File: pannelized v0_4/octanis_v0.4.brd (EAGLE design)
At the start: 69.2 x 41.9 mm, 69 parts, among them IC1 BME280, Q2 32.768kHz, U3 DRV8836DSSR, U4 DRV8836DSSR, U5 DRV8836DSSR, U7 DRV8836DSSR

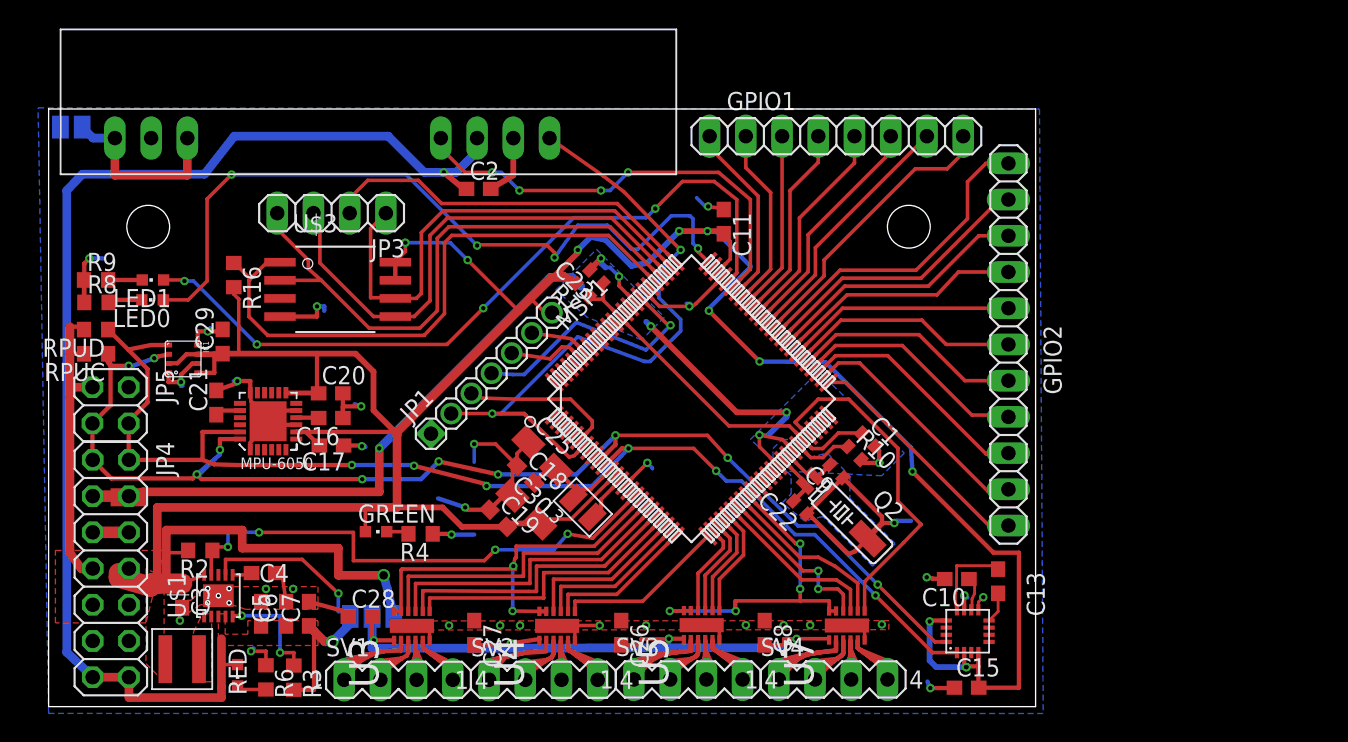
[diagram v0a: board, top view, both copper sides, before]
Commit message: corrected I2C SDA short to 3V
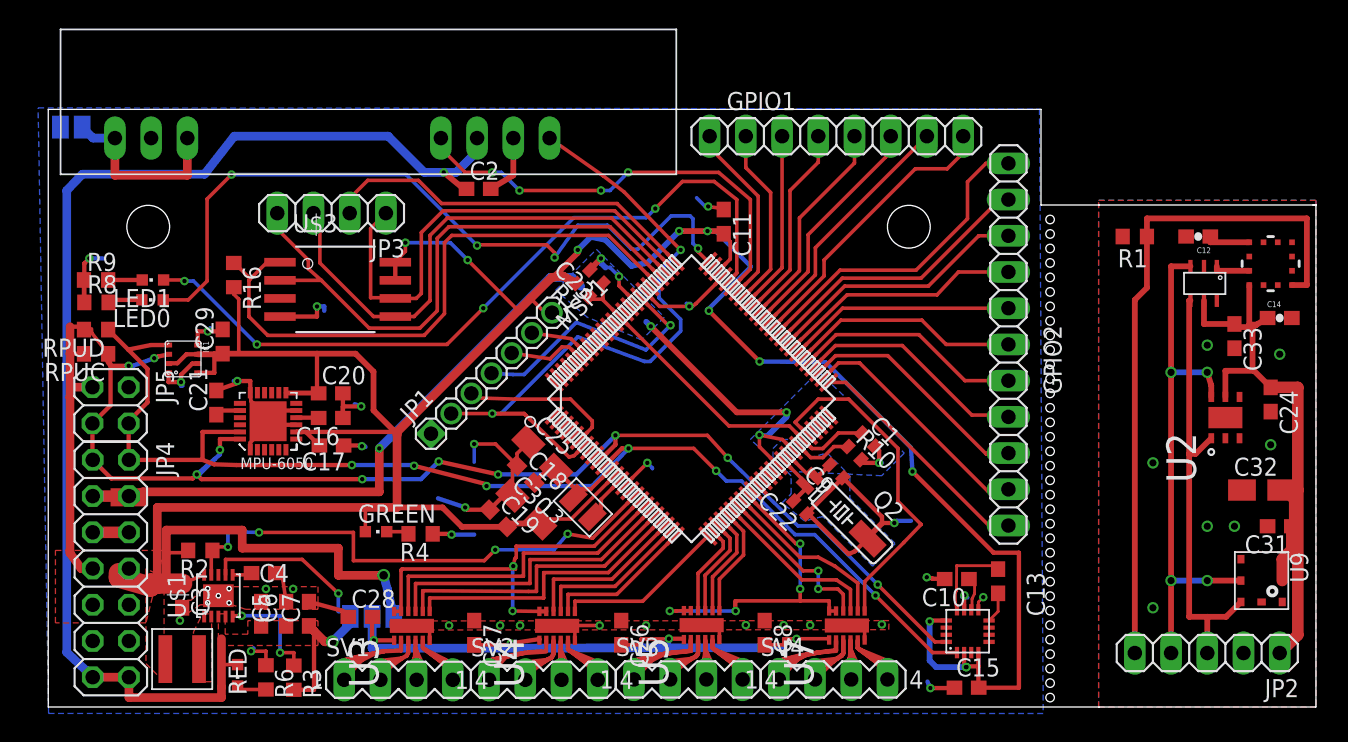
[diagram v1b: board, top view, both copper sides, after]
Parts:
- added C12: 1nF, SparkFun-Capacitors:0603-CAP
- added C14: 0.1uF, SparkFun-Capacitors:0603-CAP
- added C24, C31, C33: 100n, rcl:C0603
- added C32: 10u, resistor:A/3216-18R
- added JP2: (no value), Headerlibrary:1X05
- added R1: 10k, resistor:R0603
- added U$5: MCP3425, phMeter:SOT-23-6
- added U1: ML8511-UV-SENSOR, ML8511:ML8511
- added U2: SHT21, SENSIRION-SHT21:DFN300X300X110-7N
- added U9: BMP180, SparkFun-Sensors:BMP180
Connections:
- new net +3V1: C14.1, C24.1, C31.1, C32.+, C33.1, JP2.1, U$5.VDD, U1.7, U2.5, U9.2, U9.3
- new net GND1: C12.2, C14.2, C24.2, C31.2, C32.-, C33.2, JP2.2, R1.2, U$5.VIN-, U$5.VSS, U1.5, U2.2, U9.7
- new net N$24: C12.1, U1.10
- new net N$26: U$5.VIN+, U1.8
- new net SCL1: JP2.4, U$5.SCL, U2.6, U9.5
- new net SDA1: JP2.3, U$5.SDA, U2.1, U9.6
- new net UV_EN: JP2.5, R1.1, U1.4
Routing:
- net +3V1: track 0.00 -> 48.9 mm
- net UV_EN: track 0.00 -> 47.8 mm
- net SCL1: track 0.00 -> 37.7 mm, vias 0 -> 4
- net SDA1: track 0.00 -> 30.9 mm
- net N$24: track 0.00 -> 3.14 mm
- net N$26: track 0.00 -> 2.59 mm
- net SDA: track 90.1 -> 92.3 mm
- added copper zone on layer 1, net GND1
- added copper zone on layer 16, net GND1
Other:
- board size 69.2 x 41.9 mm -> 88.9 x 41.9 mm
- board text added: "3V3 GND SDA SCL UVEN"
- board text added: "MCP3425"
- board text added: "ML8511"
- board text added: "Octanis 1 weather monitor v1"
- board text added: "www.octanis.org"
